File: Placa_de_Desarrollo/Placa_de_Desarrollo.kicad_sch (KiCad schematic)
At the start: 43 parts, among them J1 SD_Card, J10 5V, J11 3.3V, J12 ADC_VREF, J13 GND, J14 AGND, J15 VSYS, J16 3V3_EN, J2 DEVICE I2C1, J3 DEVICE I2C0, J4 Conn_01x01, J5 Conn_01x01, J6 Conn_01x01, J7 Conn_01x01, J8 Conn_01x01, J9 Conn_01x01, U1 Pico, U2 LCD-016N002L

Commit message: Adicion de proyectos anteriores
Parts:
- removed J2: DEVICE I2C1, symbol Connector_Generic:Conn_01x04
- removed R11, R12: 4,7k, symbol Device:R
- added J17: DEVICE I2C0, symbol Connector_Generic:Conn_01x04
- added J2: Conn_01x06, symbol Connector_Generic:Conn_01x06
- added JP5, JP6, JP7, JP8: Jumper_2_Bridged, symbol Jumper:Jumper_2_Bridged
- added R13, R14: 4,7k, symbol Device:R
- J10: value 5V -> 5V_OUT
- J11: value 3.3V -> 3.3V_OUT
- J4, J5, J6, J7, J8, J9: value Conn_01x01 -> GND
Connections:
- net 3.3V: now also J17.1 (Pin_1), R13.1, R14.1
- net GND: now also J17.2 (Pin_2); no longer J4.1 (Pin_1), J5.1 (Pin_1), J6.1 (Pin_1), J7.1 (Pin_1), J8.1 (Pin_1), J9.1 (Pin_1), U1.13 (GND), U1.18 (GND), U1.23 (GND), U1.28 (GND), U1.3 (GND), U1.8 (GND)
- net SCL0: now also JP5.1 (A); no longer R9.2
- net SCL1: now also J17.4 (Pin_4), JP7.1 (A)
- net SDA0: now also JP6.1 (A); no longer R10.2
- net SDA1: now also J17.3 (Pin_3), JP8.1 (A)
- new net: J7.1 (Pin_1), U1.13 (GND)
- new net: JP5.2 (B), R9.2
- new net: J5.1 (Pin_1), U1.23 (GND)
- new net: J8.1 (Pin_1), U1.18 (GND)
- new net: J4.1 (Pin_1), U1.28 (GND)
- new net: J9.1 (Pin_1), U1.3 (GND)
- new net: J6.1 (Pin_1), U1.8 (GND)
- new net: JP6.2 (B), R10.2
- new net: JP8.2 (B), R14.2
- new net: JP7.2 (B), R13.2
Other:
- moved on the sheet: J3

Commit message: Actualizacion del Placa de Desarrollo 31/5/2025
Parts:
- removed J2: Conn_01x06, symbol Connector_Generic:Conn_01x06
- removed RV3: Contraste, symbol Device:R_Potentiometer
- removed U2: LCD-016N002L, Display:LCD-016N002L, symbol Display_Character:LCD-016N002L
- added J18: PINES GPIO, symbol Connector_Generic:Conn_01x11
- J15: value VSYS -> VSYS_ALIMEANTACION_EXTERNA
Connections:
- net 3.3V: now also J18.9 (Pin_9)
- net GND: now also J18.10 (Pin_10)
- net GPIO22: now reaches U1.29 (GPIO22)
- net GPIO22: now also J18.7 (Pin_7)
- net D4 renamed SCK/GPIO2
- net SCK/GPIO2: now also J18.3 (Pin_3)
- net D5 renamed TX/GPIO3
- net TX/GPIO3: now also J18.4 (Pin_4)
- net D6 renamed RX/GPIO4
- net RX/GPIO4: now also J18.5 (Pin_5)
- net D7 renamed CSn/GPIO5
- net CSn/GPIO5: now also J18.6 (Pin_6)
- net E renamed GPIO1
- net GPIO1: now also J18.2 (Pin_2)
- net RS renamed GPIO0
- net GPIO0: now also J18.1 (Pin_1)
- new net 5V: J18.11 (Pin_11)
- no-connect marks 15 -> 8
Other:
- note added: "CABLE VIOLETA SDA1 CABLE AMARILLO SCK1"
- note added: "GPIO PARA USO GENERAL"
- note added: "NOTA1:LOS LEDD SE ENCIENDEN CON 0 LOGICO NOTA2:LOS PINES CONECTADO A SLOS LED TAMBIEN GENERAN PWM POR LO QUE SE LOS PUEDE USAR PARA CONTROLAR LA INTENSIDAD DEL BRILLO DEL LED NOTA3: PARA EVITAR RUUIDO AGREGAR UN CAPACITOR DE 100 nF ENTRE EL PIN MEDIO Y GND NOTA4:LOS PINES DE LA PICO TIENEn RESSITENCIA PULL-UP Y PULL-DOWN INTERNOS."
- note removed: "LCD 16x2"
- note removed: "NOTA1:LOS LEDD SE ENCIENDEN CON 0 LOGICO NOTA2:LOS PINES CONECTADO A SLOS LED TAMBIEN GENERAN PWM POR LO QUE SE LOSPUEDE USAR PARA CONTROLAR LA INTENSIDAD DEL BRILLO DEL LED NOTA3: PARA EVITAR RUUIDO AGREGAR UN CAPACITOR DE 100 nF ENTRE EL PIN MEDIO Y GND NOTA4:LOS PINES DE LA PICO TIENEn RESSITENCIA PULL-UP Y PULL-DOWN INTERNOS."
- moved on the sheet: D1, D2, D3, D4, R1, R2, R3, R4

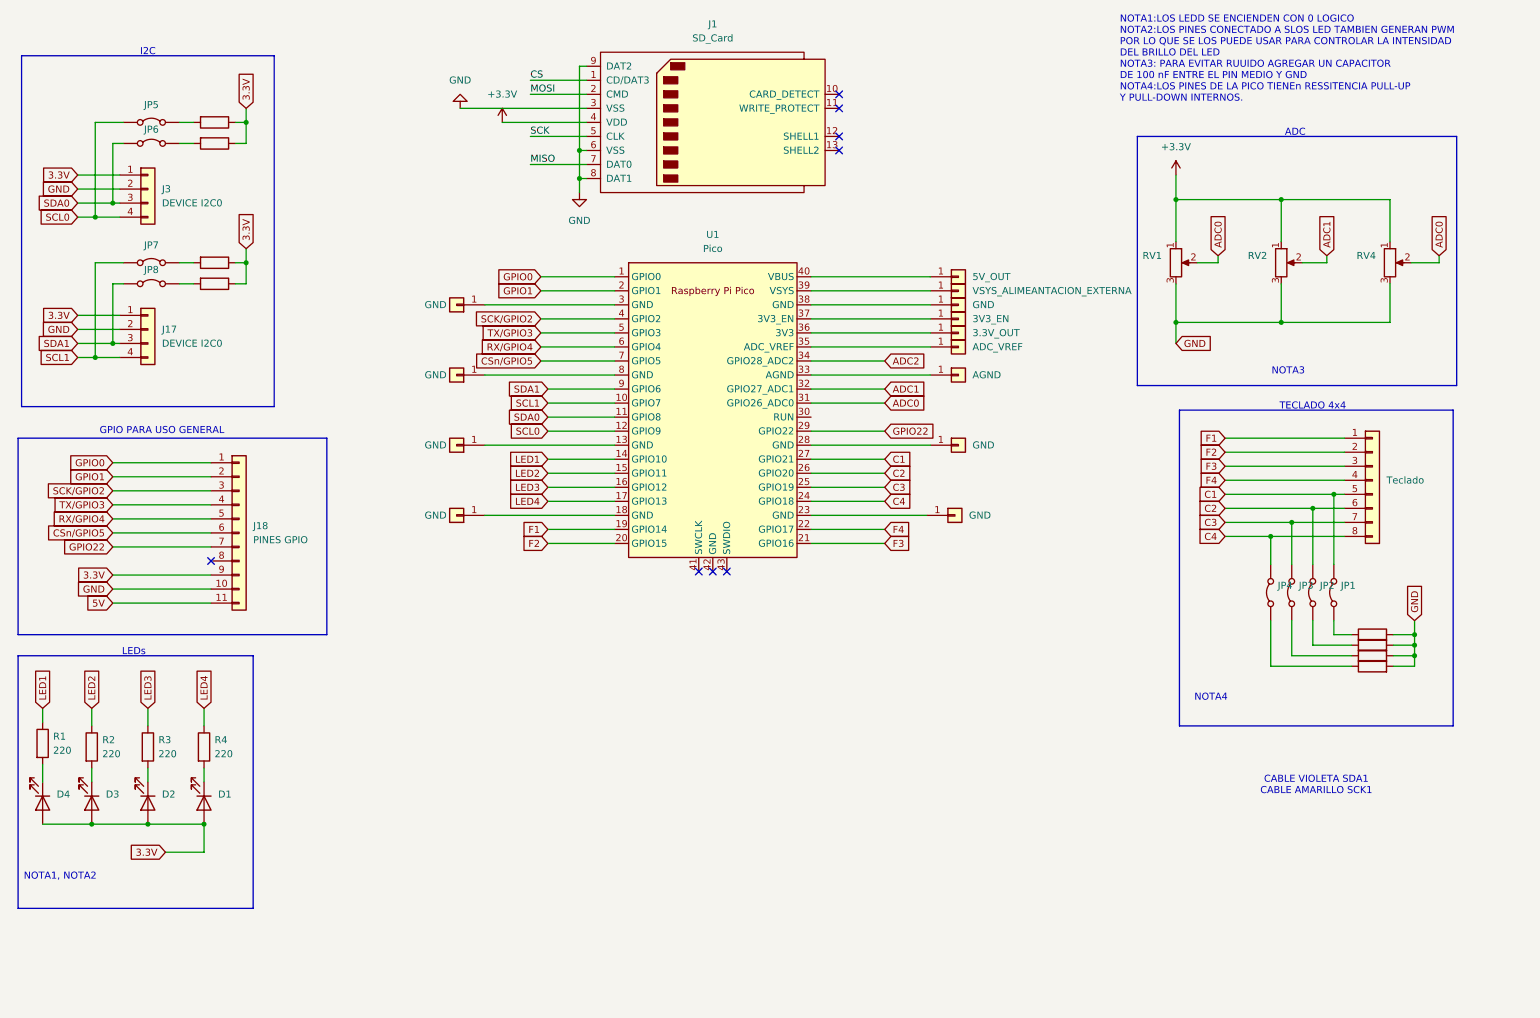
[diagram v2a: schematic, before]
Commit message: Agreggado de fuente al proyecto Placa_de_Desarrolo
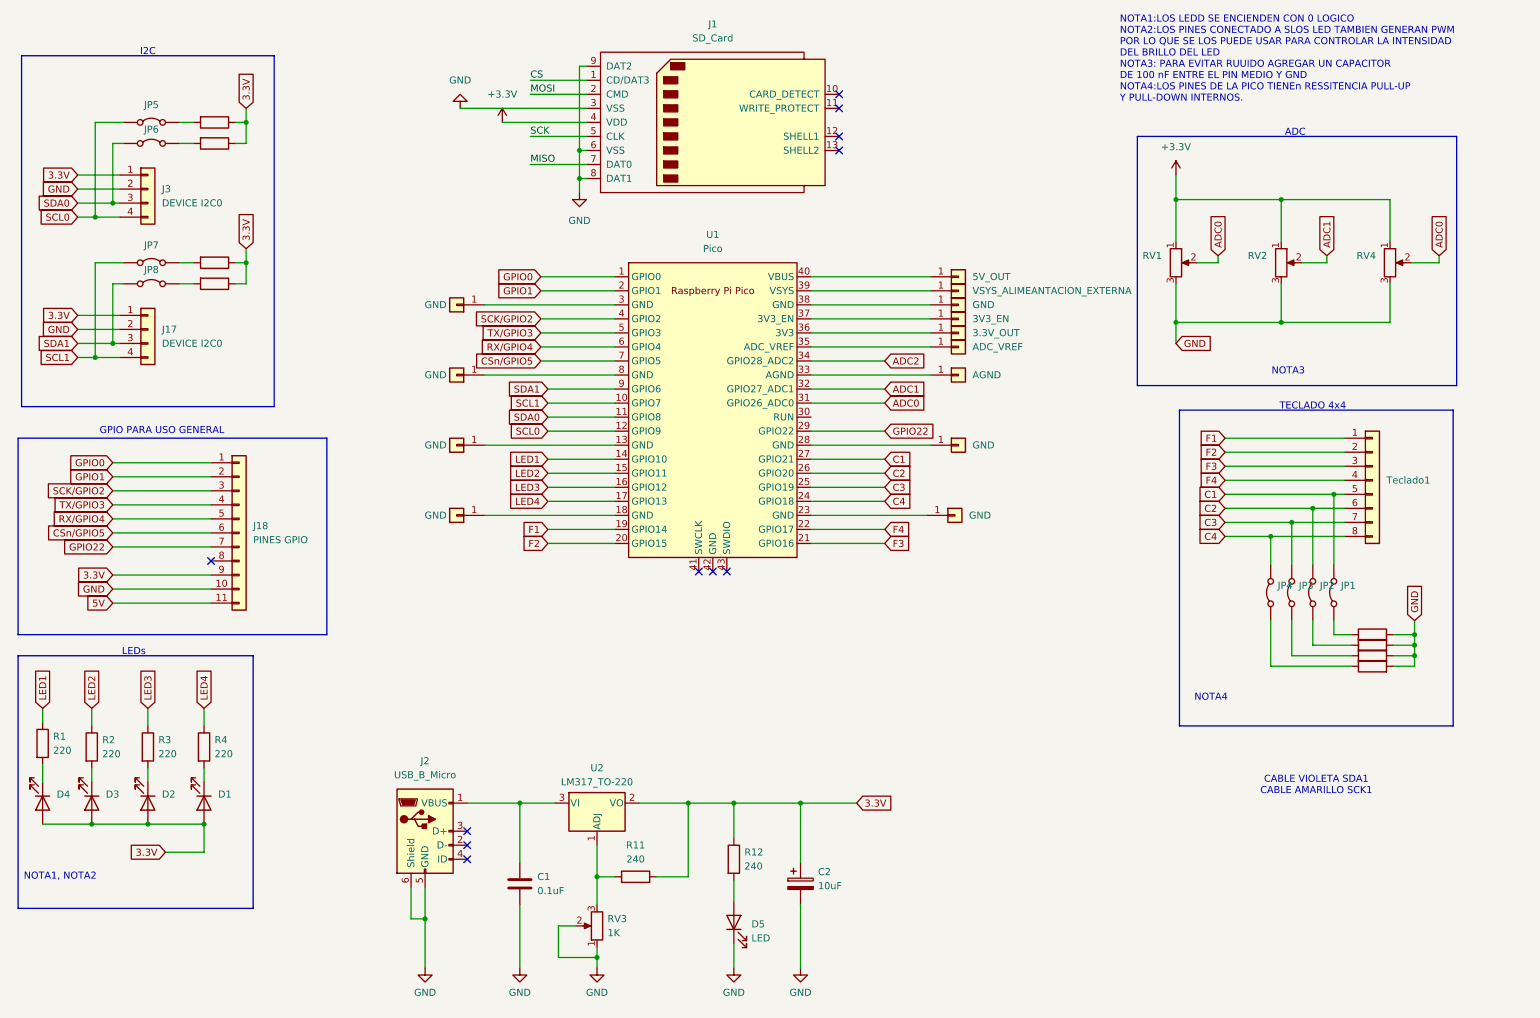
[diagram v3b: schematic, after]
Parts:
- added C1: 0.1uF, symbol Device:C
- added C2: 10uF, symbol Device:C_Polarized
- added D5: LED, symbol Device:LED
- added J2: USB_B_Micro, symbol Connector:USB_B_Micro
- added R11, R12: 240, symbol Device:R
- added RV3: 1K, symbol Device:R_Potentiometer
- added U2: LM317_TO-220, Package_TO_SOT_THT:TO-220-3_Vertical, symbol Regulator_Linear:LM317_TO-220
- renumbered Teclado to Teclado1
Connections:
- net 3.3V: now also C2.1, R11.2, R12.1, U2.2 (VO)
- net GND: now also C1.2, C2.2, D5.1 (K), J2.5 (GND), J2.6 (Shield), RV3.1, RV3.2
- new net: R11.1, RV3.3, U2.1 (ADJ)
- new net: D5.2 (A), R12.2
- new net: C1.1, J2.1 (VBUS), U2.3 (VI)
- no-connect marks 8 -> 11

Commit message: Placa_de_Desarrollo_7_6_2025
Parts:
- removed D1: LED, symbol Device:LED
- removed J1: SD_Card, symbol Connector:SD_Card
- removed R4: 220, symbol Device:R
- removed RV1, RV2, RV4: R_Potentiometer, symbol Device:R_Potentiometer
- added BZ1: Buzzer, symbol Device:Buzzer
- added J19: ADC1, symbol Connector_Generic:Conn_01x05
- added J20: ADC2, symbol Connector_Generic:Conn_01x05
- added J21: ADC0, symbol Connector_Generic:Conn_01x05
- added R15: 100, symbol Device:R
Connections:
- net +3.3V: now also J19.5 (Pin_5), J20.5 (Pin_5), J21.5 (Pin_5)
- net ADC0: now also J20.3 (Pin_3), J21.3 (Pin_3)
- net ADC1: now also J19.3 (Pin_3)
- net GND: now also BZ1.2 (-), J19.1 (Pin_1), J20.1 (Pin_1), J21.1 (Pin_1)
- net GPIO22 renamed BUZZER
- net BUZZER: now also R15.1; no longer J18.7 (Pin_7)
- net LED4 renamed GPIO13
- net GPIO13: now also J18.7 (Pin_7)
- new net: BZ1.1 (+), R15.2
- no-connect marks 11 -> 13
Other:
- note added: "NOTA1:LOS LEDD SE ENCIENDEN CON 0 LOGICO NOTA2:LOS PINES CONECTADO A SLOS LED TAMBIEN GENERAN PWM POR LO QUE SE LOS PUEDE USAR PARA CONTROLAR LA INTENSIDAD DEL BRILLO DEL LED NOTA3: PARA EVITAR RUUIDO AGREGAR UN CAPACITOR DE 100 nF ENTRE EL PIN MEDIO Y GND, EN EETE CASO USAMOS SOCALOS HEMBRA NOTA4:LOS PINES DE LA PICO TIENEn RESSITENCIA PULL-UP Y PULL-DOWN INTERNOS."
- note removed: "NOTA1:LOS LEDD SE ENCIENDEN CON 0 LOGICO NOTA2:LOS PINES CONECTADO A SLOS LED TAMBIEN GENERAN PWM POR LO QUE SE LOS PUEDE USAR PARA CONTROLAR LA INTENSIDAD DEL BRILLO DEL LED NOTA3: PARA EVITAR RUUIDO AGREGAR UN CAPACITOR DE 100 nF ENTRE EL PIN MEDIO Y GND NOTA4:LOS PINES DE LA PICO TIENEn RESSITENCIA PULL-UP Y PULL-DOWN INTERNOS."

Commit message: Actualizacion del proyecto Placa de Desarrollo 14_6_2025
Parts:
- removed JP1, JP2, JP3, JP4: Jumper_2_Bridged, symbol Jumper:Jumper_2_Bridged
- removed R5, R6, R7, R8: 10K, symbol Device:R
- added SW1, SW2: RESET, symbol Switch:SW_Push
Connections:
- net 3.3V: now also SW2.1
- net F1: now also SW2.2
- net GND: now also SW1.2
- net at U1.30 (RUN): now also SW1.1
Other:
- note added: "NOTA1:LOS LEDD SE ENCIENDEN CON 0 LOGICO NOTA2:LOS PINES CONECTADO A SLOS LED TAMBIEN GENERAN PWM POR LO QUE SE LOS PUEDE USAR PARA CONTROLAR LA INTENSIDAD DEL BRILLO DEL LED NOTA3: PARA EVITAR RUUIDO AGREGAR UN CAPACITOR DE 100 nF ENTRE EL PIN MEDIO Y GND, EN EETE CASO USAMOS SOCALOS HEMBRA"
- note removed: "NOTA1:LOS LEDD SE ENCIENDEN CON 0 LOGICO NOTA2:LOS PINES CONECTADO A SLOS LED TAMBIEN GENERAN PWM POR LO QUE SE LOS PUEDE USAR PARA CONTROLAR LA INTENSIDAD DEL BRILLO DEL LED NOTA3: PARA EVITAR RUUIDO AGREGAR UN CAPACITOR DE 100 nF ENTRE EL PIN MEDIO Y GND, EN EETE CASO USAMOS SOCALOS HEMBRA NOTA4:LOS PINES DE LA PICO TIENEn RESSITENCIA PULL-UP Y PULL-DOWN INTERNOS."
- note removed: "NOTA4"
